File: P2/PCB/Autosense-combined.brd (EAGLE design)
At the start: 100 x 41.9 mm, 24 parts, among them IC1 MC1458, K1 G6H2-100

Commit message: xwoofer crossover with 24db/octave and star ground
xwoofer routed, design rules passed, not pretty
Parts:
- removed C2A, C2B, C5: 100n, rcl:C0805
- removed C6: 2n, rcl:C0805
- removed R1A, R3: 10k, resistor:R0805
- removed R1B: 10k, rcl:M0805
- removed R7, R8: 15k, resistor:R0805
- added C3-1, C3-2, CA-1, CA-2, CB-1, CB-2: 100n, rcl:C0805
- added C4-2, C5-1, C5-2: 2n, rcl:C0805
- added D1-2: (no value), diode:GF1
- added IC2: MC1458, burr-brown:SO08
- added K2: G6H2-100, relay:G6H2-100
- added R3-1, R3-2, RA-1, RA-2: 10k, resistor:R0805
- added R7-1, R7-2, R8-1, R8-2: 5k, resistor:R0805
- added RB-1, RB-2: 10k, rcl:M0805
- R1: device rcl:R0805 -> rcl:R1206
- moved R1 16.8 mm to (1.91, 10.2), turned to 90 degrees
- moved R6 3.81 mm to (10.2, 24.1)
- moved IC1 3.81 mm to (90.2, 8.26)
- flipped R5 to the bottom, turned to 180 degrees
- renumbered C4 to C4-1, D1 to D1-1
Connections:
- removed net J1: D1-1.A, K1.10
- removed net J2: C4-1.1, IC1.6, IC1.7
- removed net N$15: K1.S2, OUT1.1
- removed net N$16: K1.S1, OUT1.3
- removed net N$3: OUT1.2, OUT1.4, R1.2, X1.2
- new net $NET1: CB-2.1, K2.P1, X2.1
- new net ADC0: C4-1.1, CON1.9, IC1.6, IC1.7
- new net ADC1: C4-2.1, CON1.7, IC2.6, IC2.7
- new net ADC2: CON1.5
- new net ADC3: CON1.3
- new net AGND: C1.2, C5-1.2, C5-2.2, CON1.12, OUT1.2, OUT1.4, R1.2, R5.1, X1.2, X2.2
- new net N$10: IC2.2, R3-2.1, RA-2.1, RB-2.1
- new net N$12: C5-2.1, IC2.5, R8-2.1
- new net N$14: C4-2.2, R7-2.1, R8-2.2
- new net N$17: CA-2.2, RA-2.2
- new net N$18: CB-2.2, RB-2.2
- new net N$19: CA-2.1, K2.P2, X2.3
- new net N$7: IC2.1, R3-2.2, R7-2.2
- new net OUT0: CON1.10, D1-1.A, K1.10
- new net OUT1: CON1.8, D1-2.A, K2.10
- new net OUT1-1: K1.S2, K2.S2, OUT1.1
- new net OUT1-3: K1.S1, K2.S1, OUT1.3
- new net OUT2: CON1.6
- new net OUT3: CON1.4
- net $NET13: now also CB-1.1; no longer C2B.1
- net 5V: now also C3-1.1, C3-2.1, D1-2.C, IC2.8, K2.1; no longer C5.1
- net GND: now also C3-1.2, C3-2.2, IC2.4; no longer C1.2, C5.2, C6.2, R5.1
- net N$1: now also CA-1.1; no longer C2A.1
- net N$11: now also CA-1.2, RA-1.2; no longer C2A.2, R1A.2
- net N$13: now also CB-1.2, RB-1.2; no longer C2B.2, R1B.2
- net N$2: now also C5-1.1, R8-1.1; no longer C6.1, R8.1
- net N$6: now also R3-1.1, RA-1.1, RB-1.1; no longer R1A.1, R1B.1, R3.1
- net N$8: now also R7-1.1, R8-1.2; no longer R7.1, R8.2
- net N$9: now also R3-1.2, R7-1.2; no longer R3.2, R7.2
- net V/2: now also IC2.3
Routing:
- net AGND: track 0.00 -> 186.3 mm
- net V/2: track 33.6 -> 164.4 mm, vias 0 -> 2
- net N$3: track 109.3 -> 0.00 mm
- net OUT0: track 0.00 -> 109.2 mm
- net OUT1-3: track 0.00 -> 100.4 mm, vias 0 -> 1
- net OUT1-1: track 0.00 -> 94.7 mm, vias 0 -> 2
- net N$16: track 91.5 -> 0.00 mm
- net OUT1: track 0.00 -> 90.7 mm
- net N$15: track 76.0 -> 0.00 mm, vias 1 -> 0
- net 5V: track 146.3 -> 181.9 mm
- net N$19: track 0.00 -> 26.1 mm
- net $NET1: track 0.00 -> 19.4 mm
- net N$10: track 0.00 -> 18.2 mm
- net $NET13: track 34.9 -> 19.9 mm
- net N$12: track 0.00 -> 13.3 mm, vias 0 -> 1
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
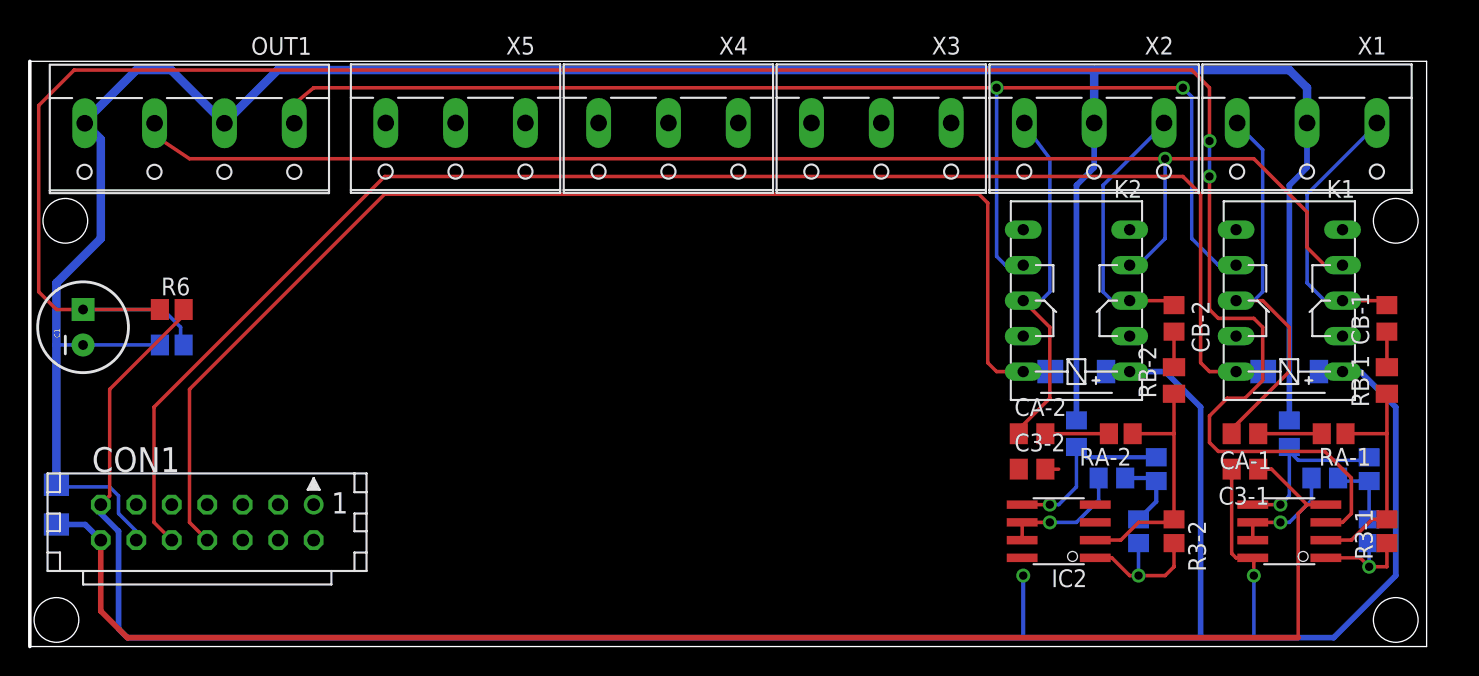
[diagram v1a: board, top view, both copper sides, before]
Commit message: Autosense 4+1 channels complete
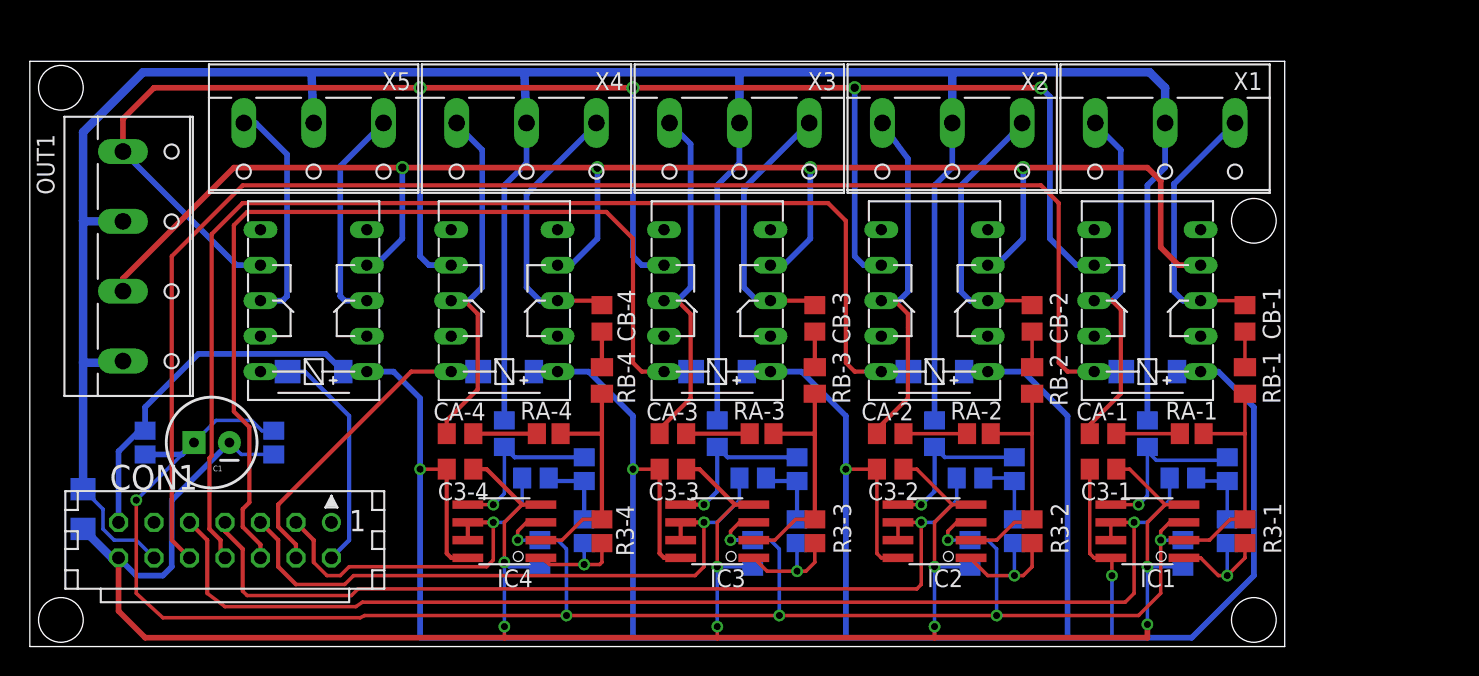
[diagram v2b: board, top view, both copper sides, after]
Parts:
- added C3-3, C3-4, CA-3, CA-4, CB-3, CB-4, CV-1, CV-2, CV-3, CV-4: 100n, rcl:C0805
- added C4-3, C4-4, C5-3, C5-4: 2n, rcl:C0805
- added D1-3, D1-4, D1-5: (no value), diode:GF1
- added IC3, IC4: MC1458, burr-brown:SO08
- added K3, K4, K5: G6H2-100, relay:G6H2-100
- added R3-3, R3-4, RA-3, RA-4: 10k, resistor:R0805
- added R7-3, R7-4, R8-3, R8-4: 5k, resistor:R0805
- added RB-3, RB-4: 10k, rcl:M0805
- moved C1 12.4 mm to (13.0, 14.6), turned to 180 degrees
- moved C3-1 10.2 mm to (76.8, 12.7)
- moved C5-2 10.2 mm to (64.8, 15.2)
- moved CA-1 10.2 mm to (76.8, 15.2)
- moved CB-2 10.2 mm to (71.8, 23.5)
- moved D1-2 10.2 mm to (64.8, 19.7)
- moved K2 10.2 mm to (64.8, 24.8)
- moved R3-2 10.2 mm to (71.8, 8.26)
- moved R7-1 10.2 mm to (85.7, 8.26)
- moved R8-1 10.2 mm to (85.7, 12.7)
- moved RA-2 10.2 mm to (67.9, 15.2)
- moved RB-2 10.2 mm to (71.8, 19.1)
- moved X3 10.2 mm to (50.8, 36.2)
- moved X5 10.2 mm to (20.3, 36.2)
- moved C3-2 10.2 mm to (61.6, 12.7)
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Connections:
- removed net OUT1-1: K1.S2, K2.S2, OUT1.1
- new net $NET2: CB-3.1, K3.P1, X3.1
- new net $NET3: CB-4.1, K4.P1, X4.1
- new net $NET4: K5.P1, X5.1
- new net N$15: C4-3.2, R7-3.1, R8-3.2
- new net N$16: CA-3.2, RA-3.2
- new net N$20: CB-3.2, RB-3.2
- new net N$21: CA-3.1, K3.P2, X3.3
- new net N$22: IC4.1, R3-4.2, R7-4.2
- new net N$23: IC4.2, R3-4.1, RA-4.1, RB-4.1
- new net N$24: C5-4.1, IC4.5, R8-4.1
- new net N$25: C4-4.2, R7-4.1, R8-4.2
- new net N$26: CA-4.2, RA-4.2
- new net N$27: CB-4.2, RB-4.2
- new net N$28: CA-4.1, K4.P2, X4.3
- new net N$29: K5.P2, X5.3
- new net N$3: IC3.1, R3-3.2, R7-3.2
- new net N$4: IC3.2, R3-3.1, RA-3.1, RB-3.1
- new net N$5: C5-3.1, IC3.5, R8-3.1
- new net OUT1-2: K1.S2, K2.S2, K3.S2, K4.S2, K5.S2, OUT1.1
- new net OUT4: CON1.2, D1-5.A, K5.10
- net 5V: now also C3-3.1, C3-4.1, D1-3.C, D1-4.C, D1-5.C, IC3.8, IC4.8, K3.1, K4.1, K5.1
- net ADC2: now also C4-3.1, IC3.6, IC3.7
- net ADC3: now also C4-4.1, IC4.6, IC4.7
- net AGND: now also C5-3.2, C5-4.2, X3.2, X4.2, X5.2; no longer C1.2, R5.1
- net GND: now also C1.2, C3-3.2, C3-4.2, CV-1.1, CV-2.1, CV-3.1, CV-4.1, IC3.4, IC4.4, R5.1
- net OUT1-3: now also K3.S1, K4.S1, K5.S1
- net OUT2: now also D1-3.A, K3.10
- net OUT3: now also D1-4.A, K4.10
- net V/2: now also CV-1.2, CV-2.2, CV-3.2, CV-4.2, IC3.3, IC4.3
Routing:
- net OUT1-2: track 0.00 -> 140.6 mm, vias 0 -> 4
- net OUT1-1: track 94.7 -> 0.00 mm, vias 2 -> 0
- net ADC0: track 7.72 -> 85.4 mm
- net OUT2: track 0.00 -> 68.1 mm
- net 5V: track 181.9 -> 246.6 mm, vias 2 -> 4
- net GND: track 111.9 -> 174.5 mm, vias 0 -> 8
- net ADC1: track 8.99 -> 66.6 mm
- net ADC2: track 0.00 -> 46.1 mm, vias 0 -> 1
- net AGND: track 186.3 -> 223.6 mm
- net ADC3: track 0.00 -> 27.4 mm, vias 0 -> 1
- net N$28: track 0.00 -> 26.9 mm
- net N$21: track 0.00 -> 26.5 mm
- net V/2: track 164.4 -> 140.5 mm, vias 2 -> 8
- net OUT3: track 0.00 -> 22.6 mm
- net OUT1-3: track 100.4 -> 121.3 mm, vias 1 -> 4
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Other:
- board size 100 x 41.9 mm -> 89.8 x 41.9 mm
